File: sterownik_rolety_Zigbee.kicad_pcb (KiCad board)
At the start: 2 copper layers, 39 parts, among them J1 282836-5, J2 1725669, J3 53398-0567, Q1 BT136-600, Q2 BT136-600, Q3 MOC3032M, Q4 MOC3032M, U1 LTV-817, U2 LTV-817, U3 IRM-01-3.3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

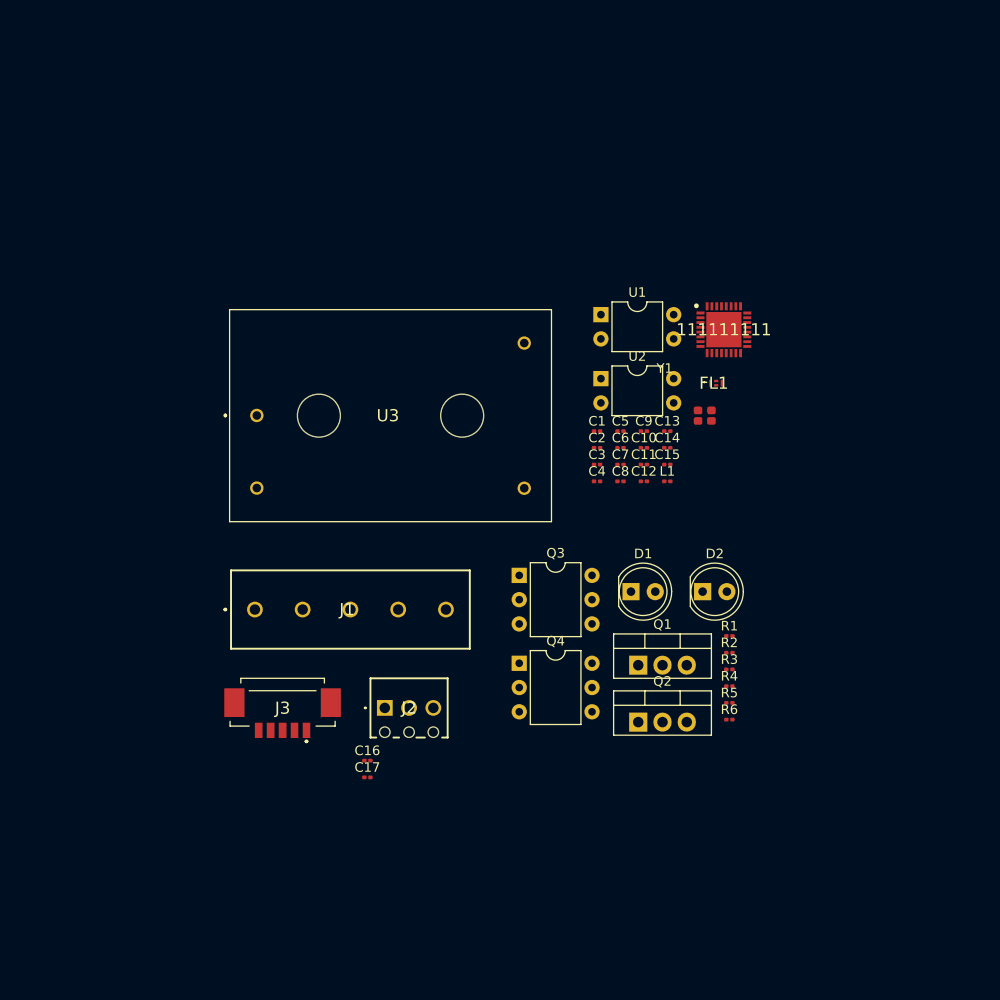
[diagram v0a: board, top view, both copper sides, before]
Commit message: początkowe rozłożenie na PCB
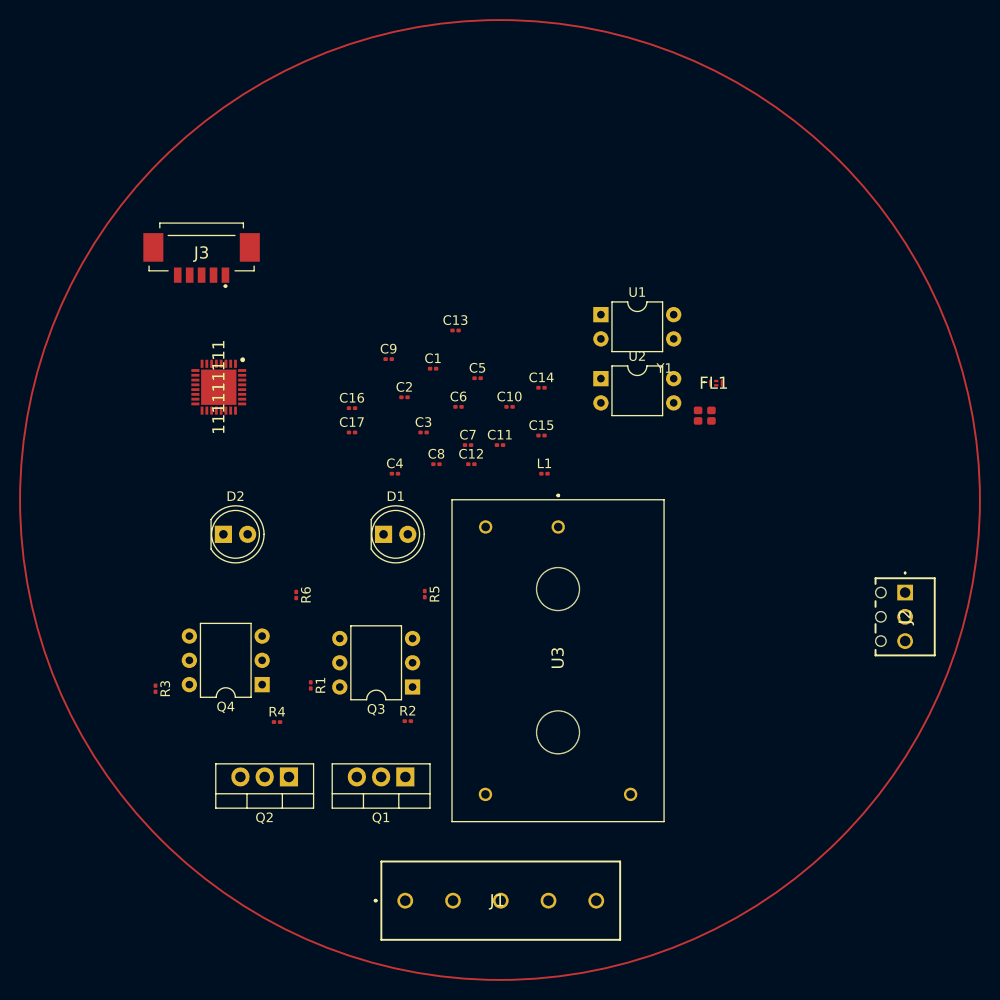
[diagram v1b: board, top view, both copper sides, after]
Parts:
- R5: value 330 -> 330R
- R6: value 200 -> 330R
- moved R3 60.1 mm to (90.9, 117.5), turned to -90 degrees
- moved J2 55.8 mm to (169.4, 107.4), turned to -90 degrees
- moved 111111111 53.2 mm to (97.6, 85.9), turned to -90 degrees
- moved D2 50.5 mm to (98.0, 101.3)
- moved J3 48.4 mm to (95.8, 71.9)
- moved R4 47.5 mm to (103.7, 121.0)
- moved R6 47.2 mm to (105.7, 107.7), turned to -90 degrees
- moved R1 44.1 mm to (107.2, 117.2), turned to -90 degrees
- moved Q2 37.0 mm to (104.9, 126.7), turned to 180 degrees
- moved C16 36.9 mm to (111.5, 88.1)
- moved C17 36.2 mm to (111.5, 90.7)
- moved R2 34.4 mm to (117.3, 120.9)
- moved J1 34.3 mm to (117.1, 139.7)
- moved R5 33.9 mm to (119.1, 107.6), turned to -90 degrees
- moved U3 33.6 mm to (133.1, 100.6), turned to -90 degrees
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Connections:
- J1 pad 3: Q_L_connector -> N_connector
- J1 pad 4: L_connector -> N_connector
- J1 pad 5: N_connector -> L_connector
- Q1 pad 1: 230_L_Connector -> L_connector
- Q2 pad 1: 230_L_Connector -> L_connector
- R2 pad 2: 230_L_Connector -> L_connector
- R4 pad 2: 230_L_Connector -> L_connector
- U3 pad 3: 230_N_Connector -> N_connector
- U3 pad 4: 230_L_Connector -> L_connector

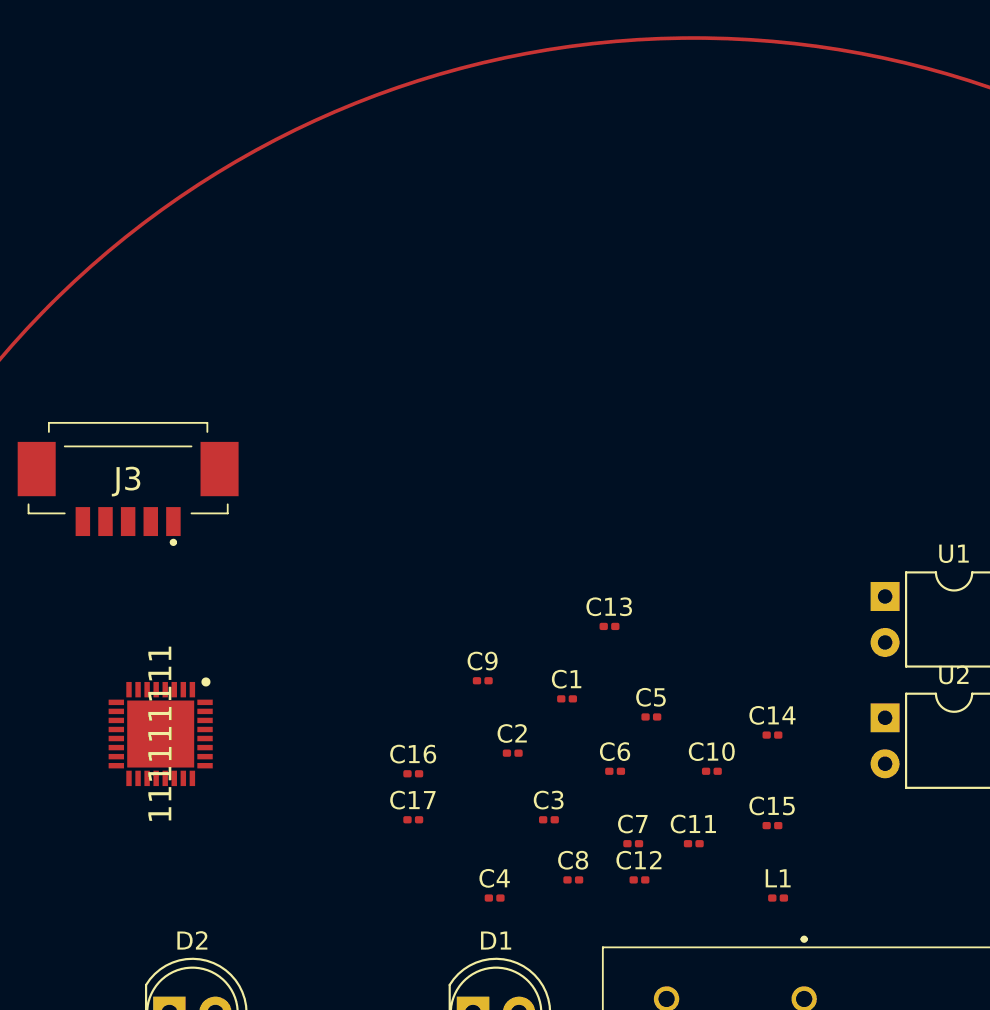
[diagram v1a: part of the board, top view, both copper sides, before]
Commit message: Update sterownik_rolety_Zigbee.kicad_pcb
większe R i C, dodana antena
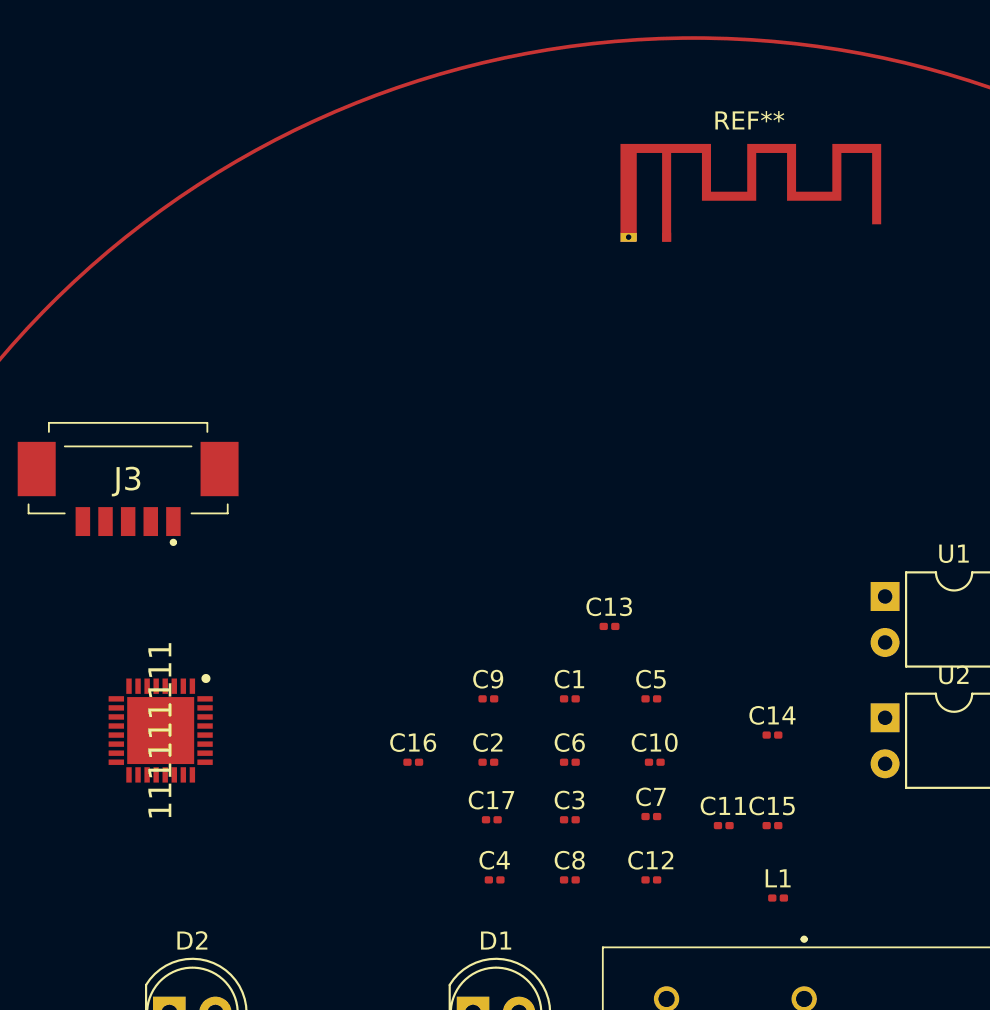
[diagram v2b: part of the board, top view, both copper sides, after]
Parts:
- added REF**: Texas_SWRA117D_2.4GHz_Right, RF_Antenna:Texas_SWRA117D_2.4GHz_Right, F.Cu at (125.5, 58.5)
- moved C17 4.34 mm to (115.8, 90.7)
- moved C10 3.19 mm to (124.8, 87.5)
- moved C6 2.55 mm to (120.2, 87.5)
- moved C11 1.93 mm to (128.7, 91.0)
- moved C7 1.80 mm to (124.7, 90.5)
- moved C2 1.43 mm to (115.7, 87.5)
- moved C3 1.16 mm to (120.2, 90.7)
- moved C9 1.05 mm to (115.7, 84.0)
- moved C4 1.00 mm to (116.0, 94.0)
- moved C5 1.00 mm to (124.7, 84.0)
- moved C12 0.66 mm to (124.7, 94.0)
- moved C16 0.64 mm to (111.5, 87.5)
- moved 111111111 0.19 mm to (97.6, 85.8)
- moved C8 0.19 mm to (120.2, 94.0)
- moved C1 0.16 mm to (120.2, 84.0)
